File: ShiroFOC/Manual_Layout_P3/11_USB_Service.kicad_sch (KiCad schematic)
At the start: 20 parts, among them J201 USB-C service, U202 USBLC6-2SC6, U901 CP2102N-A02-GQFN20

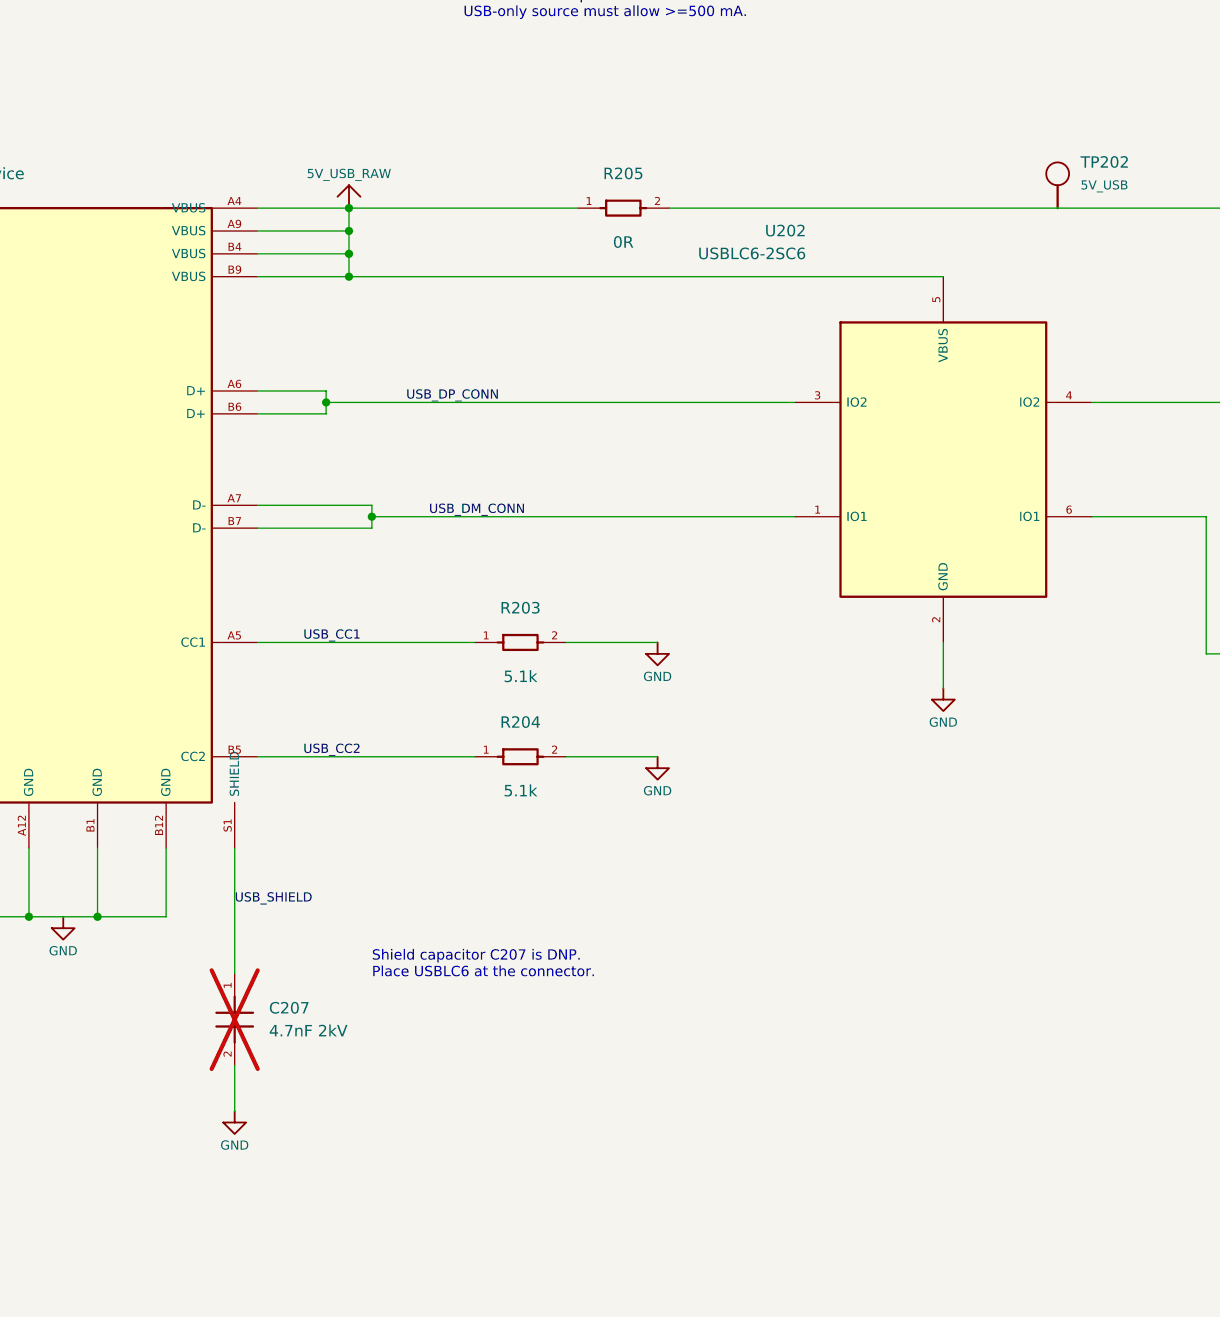
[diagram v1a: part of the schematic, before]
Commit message: usb and pwr mux
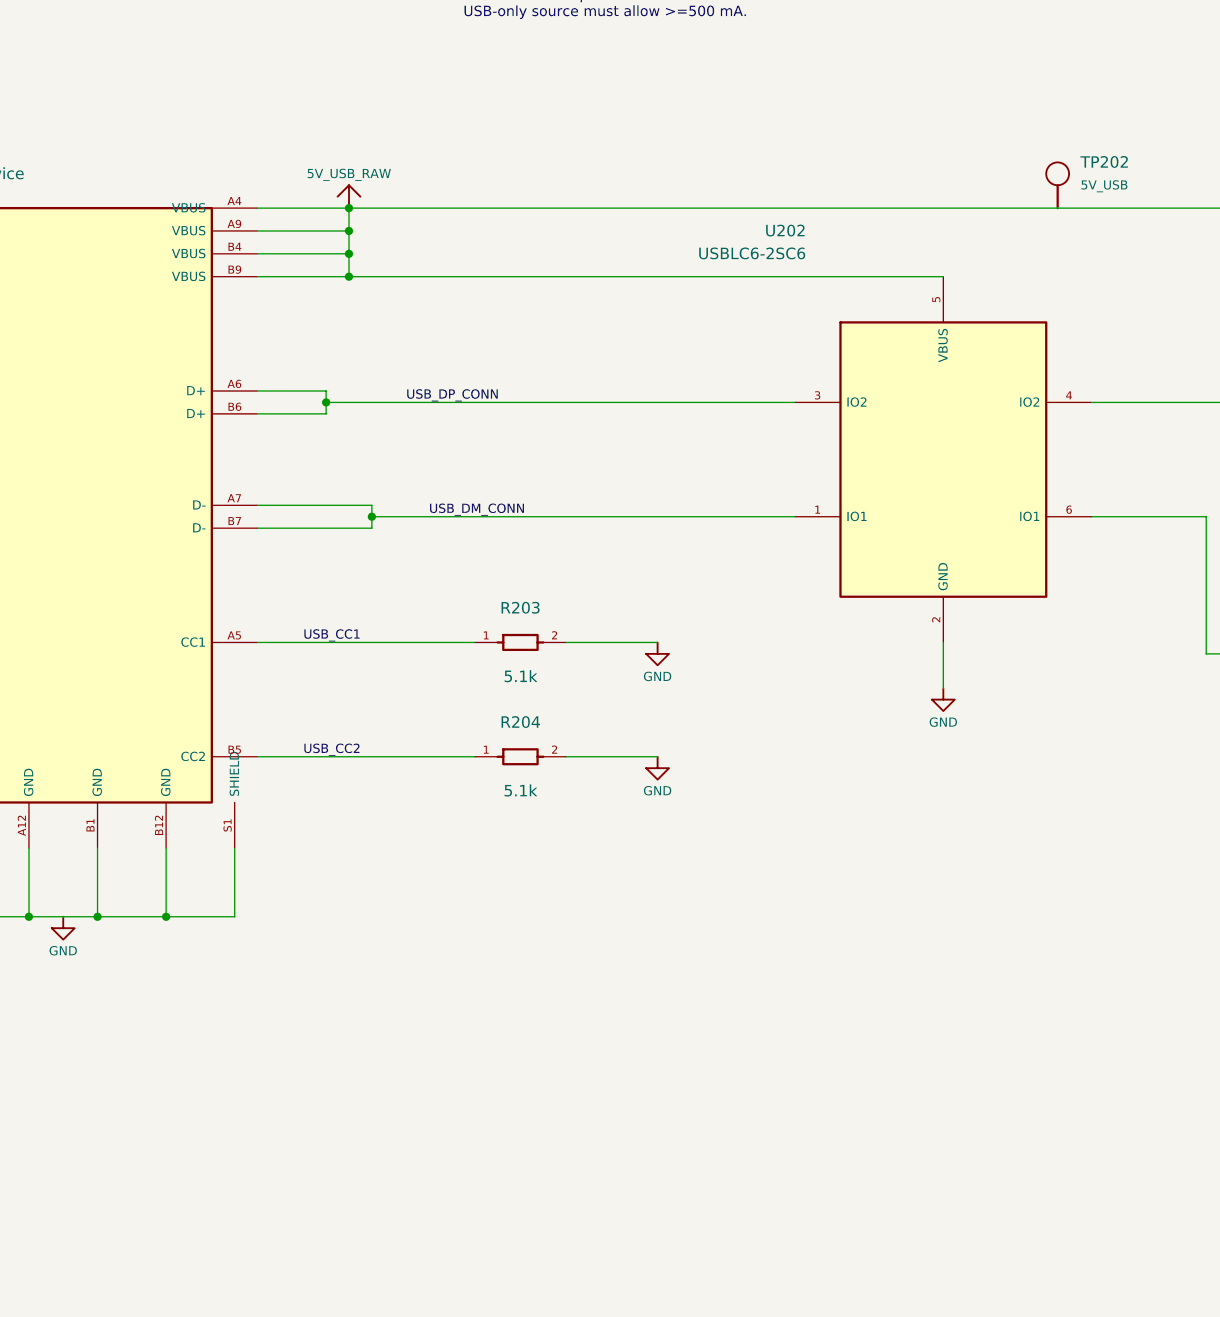
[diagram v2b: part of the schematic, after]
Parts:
- removed C207: 4.7nF 2kV, Capacitor_SMD:C_1206_3216Metric, symbol Manual:COMP_C207
- removed R205: 0R, Resistor_SMD:R_0402_1005Metric, symbol Manual:COMP_R205
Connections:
- net 5V_USB is gone; now on net 5V_USB_RAW: C208.1, TP202.1
- net USB_SHIELD is gone; now on net GND: J201.S1 (SHIELD)
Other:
- note removed: "Shield capacitor C207 is DNP. Place USBLC6 at the connector."

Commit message: CAN layout
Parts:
- C208: symbol Manual:COMP_C208 -> ShiroFOCLib:COMP_C208
- C901: symbol Manual:COMP_C901 -> ShiroFOCLib:COMP_C901
- C902: symbol Manual:COMP_C902 -> ShiroFOCLib:COMP_C902
- C903: symbol Manual:COMP_C903 -> ShiroFOCLib:COMP_C903
- C904: symbol Manual:COMP_C904 -> ShiroFOCLib:COMP_C904
- J201: symbol Manual:COMP_J201 -> ShiroFOCLib:COMP_J201
- R203: symbol Manual:COMP_R203 -> ShiroFOCLib:COMP_R203
- R204: symbol Manual:COMP_R204 -> ShiroFOCLib:COMP_R204
- R901: symbol Manual:COMP_R901 -> ShiroFOCLib:COMP_R901
- R902: symbol Manual:COMP_R902 -> ShiroFOCLib:COMP_R902
- R903: symbol Manual:COMP_R903 -> ShiroFOCLib:COMP_R903
- R904: symbol Manual:COMP_R904 -> ShiroFOCLib:COMP_R904
- R905: symbol Manual:COMP_R905 -> ShiroFOCLib:COMP_R905
- TP202: symbol Manual:COMP_TP202 -> ShiroFOCLib:COMP_TP202
- TP901: symbol Manual:COMP_TP901 -> ShiroFOCLib:COMP_TP901
- TP902: symbol Manual:COMP_TP902 -> ShiroFOCLib:COMP_TP902
- U202: footprint Manual:USBLC6_SOT23_6 -> ShiroFOCLib:USBLC6_SOT23_6; symbol Manual:COMP_U202 -> ShiroFOCLib:COMP_U202
- U901: symbol Manual:COMP_U901 -> ShiroFOCLib:COMP_U901
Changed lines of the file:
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@@
 	)
 	(symbol
-		(lib_id "Manual:COMP_C208")
+		(lib_id "ShiroFOCLib:COMP_C208")
 		(at 203.2 78.74 0)
 		(unit 1)
@@
 	)
 	(symbol
-		(lib_id "Manual:COMP_U901")
+		(lib_id "ShiroFOCLib:COMP_U901")
 		(at 285.75 116.84 0)
 		(unit 1)
@@
 	)
 	(symbol
-		(lib_id "Manual:COMP_TP202")
+		(lib_id "ShiroFOCLib:COMP_TP202")
 		(at 167.64 62.23 0)
 		(unit 1)
@@
 	)
 	(symbol
-		(lib_id "Manual:COMP_U202")
+		(lib_id "ShiroFOCLib:COMP_U202")
 		(at 154.94 90.17 0)
 		(unit 1)
@@
 			)
 		)
-		(property "Footprint" "Manual:USBLC6_SOT23_6"
+		(property "Footprint" "ShiroFOCLib:USBLC6_SOT23_6"
 			(at 154.94 107.95 0)
 			(effects
@@
 	)
 	(symbol
-		(lib_id "Manual:PWR_3V3")
+		(lib_id "ShiroFOCLib:PWR_3V3")
 		(at 234.95 119.38 0)
 		(unit 1)
@@
 	)
 	(symbol
-		(lib_id "Manual:COMP_C901")
+		(lib_id "ShiroFOCLib:COMP_C901")
 		(at 246.38 53.34 0)
 		(unit 1)
@@
 	)
 	(symbol
-		(lib_id "Manual:PWR_3V3")
+		(lib_id "ShiroFOCLib:PWR_3V3")
 		(at 285.75 43.18 0)
 		(unit 1)
@@
 	)
 	(symbol
-		(lib_id "Manual:PWR_5V_USB_RAW")
+		(lib_id "ShiroFOCLib:PWR_5V_USB_RAW")
 		(at 218.44 43.18 0)
 		(unit 1)
@@
 	)
 	(symbol
-		(lib_id "Manual:PWR_GND")
+		(lib_id "ShiroFOCLib:PWR_GND")
 		(at 218.44 86.36 0)
 		(unit 1)
@@
 	)
 	(symbol
-		(lib_id "Manual:PWR_GND")
+		(lib_id "ShiroFOCLib:PWR_GND")
 		(at 154.94 115.57 0)
 		(unit 1)
@@
 	)
 	(symbol
-		(lib_id "Manual:PWR_GND")
+		(lib_id "ShiroFOCLib:PWR_GND")
 		(at 285.75 167.64 0)
 		(unit 1)
@@
 	)
 	(symbol
-		(lib_id "Manual:COMP_C904")
+		(lib_id "ShiroFOCLib:COMP_C904")
 		(at 322.58 53.34 0)
 		(unit 1)
@@
 	)
 	(symbol
-		(lib_id "Manual:COMP_J201")
+		(lib_id "ShiroFOCLib:COMP_J201")
 		(at 57.15 95.25 0)
 		(unit 1)
@@
 	)
 	(symbol
-		(lib_id "Manual:COMP_R902")
+		(lib_id "ShiroFOCLib:COMP_R902")
 		(at 336.55 101.6 0)
 		(unit 1)
@@
 	)
 	(symbol
-		(lib_id "Manual:PWR_GND")
+		(lib_id "ShiroFOCLib:PWR_GND")
 		(at 261.62 63.5 0)
 		(unit 1)
@@
 	)
 	(symbol
-		(lib_id "Manual:PWR_5V_USB_RAW")
+		(lib_id "ShiroFOCLib:PWR_5V_USB_RAW")
 		(at 88.9 62.23 0)
 		(unit 1)
@@
 	)
 	(symbol
-		(lib_id "Manual:PWR_GND")
+		(lib_id "ShiroFOCLib:PWR_GND")
 		(at 123.19 123.19 0)
 		(unit 1)
@@
 	)
 	(symbol
-		(lib_id "Manual:PWR_GND")
+		(lib_id "ShiroFOCLib:PWR_GND")
 		(at 307.34 63.5 0)
 		(unit 1)
@@
 	)
 	(symbol
-		(lib_id "Manual:PWR_GND")
+		(lib_id "ShiroFOCLib:PWR_GND")
 		(at 246.38 63.5 0)
 		(unit 1)
@@
 	)
 	(symbol
-		(lib_id "Manual:COMP_R204")
+		(lib_id "ShiroFOCLib:COMP_R204")
 		(at 107.95 123.19 0)
 		(unit 1)
@@
 	)
 	(symbol
-		(lib_id "Manual:PWR_GND")
+		(lib_id "ShiroFOCLib:PWR_GND")
 		(at 123.19 110.49 0)
 		(unit 1)
@@
 	)
 	(symbol
-		(lib_id "Manual:COMP_TP902")
+		(lib_id "ShiroFOCLib:COMP_TP902")
 		(at 355.6 101.6 0)
 		(unit 1)
@@
 	)
 	(symbol
-		(lib_id "Manual:COMP_R904")
+		(lib_id "ShiroFOCLib:COMP_R904")
 		(at 218.44 55.88 0)
 		(unit 1)
@@
 	)
 	(symbol
-		(lib_id "Manual:PWR_GND")
+		(lib_id "ShiroFOCLib:PWR_GND")
 		(at 57.15 140.97 0)
 		(unit 1)
@@
 	)
 	(symbol
-		(lib_id "Manual:COMP_C903")
+		(lib_id "ShiroFOCLib:COMP_C903")
 		(at 307.34 53.34 0)
 		(unit 1)
@@
 	)
 	(symbol
-		(lib_id "Manual:COMP_R905")
+		(lib_id "ShiroFOCLib:COMP_R905")
 		(at 218.44 76.2 0)
 		(unit 1)
@@
 	)
 	(symbol
-		(lib_id "Manual:PWR_GND")
+		(lib_id "ShiroFOCLib:PWR_GND")
 		(at 322.58 63.5 0)
 		(unit 1)
@@
 	)
 	(symbol
-		(lib_id "Manual:PWR_GND")
+		(lib_id "ShiroFOCLib:PWR_GND")
 		(at 203.2 88.9 0)
 		(unit 1)
@@
 	)
 	(symbol
-		(lib_id "Manual:COMP_R903")
+		(lib_id "ShiroFOCLib:COMP_R903")
 		(at 336.55 111.76 0)
 		(unit 1)
@@
 	)
 	(symbol
-		(lib_id "Manual:COMP_R203")
+		(lib_id "ShiroFOCLib:COMP_R203")
 		(at 107.95 110.49 0)
 		(unit 1)
@@
 	)
 	(symbol
-		(lib_id "Manual:COMP_R901")
+		(lib_id "ShiroFOCLib:COMP_R901")
 		(at 234.95 129.54 0)
 		(unit 1)
@@
 	)
 	(symbol
-		(lib_id "Manual:COMP_TP901")
+		(lib_id "ShiroFOCLib:COMP_TP901")
 		(at 355.6 111.76 0)
 		(unit 1)
@@
 	)
 	(symbol
-		(lib_id "Manual:COMP_C902")
+		(lib_id "ShiroFOCLib:COMP_C902")
 		(at 261.62 53.34 0)
 		(unit 1)
